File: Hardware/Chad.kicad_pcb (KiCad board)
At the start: 4 copper layers, 30 x 60 mm, 127 parts, among them J1 RBUS, J2 GPIO Breakout, J3 ServoCH1, J4 ServoCH2, J5 USB_C_Receptacle_USB2.0, U1 ESP32-S3, U2 SN65HVD230, U3 LM66200DRLR, U4 MAX77827AEFD+T, U5 SC4215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

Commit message: last commit is a lie, made some small changes
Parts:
- moved LOGO1 0.56 mm to (49.4, 82.0)
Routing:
- net GND: track 24.8 -> 30.5 mm
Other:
- board text added: "JLCJLCJLCJLC"
- board text added: "Serial Number -"

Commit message: small silkscreen tweaks
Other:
- board text added: "C.H.A.D-v2.0"
- board text removed: "C.H.A.D-v2"
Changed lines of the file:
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@@
   (gr_line locked (start 62 99.09) (end 62 45.09)
     (stroke (width 0.1) (type solid)) (layer "Edge.Cuts"))
-  (gr_text "Serial Number - " (at 59.85 93.3 -90) (layer "B.SilkS")
-    (effects (font (size 0.7 0.7) (thickness 0.1524) bold) (justify left bottom mirror))
+  (gr_text "Serial Number - " (at 59.81 95.7 270) (layer "B.SilkS")
+    (effects (font (size 0.9 0.9) (thickness 0.1524) bold) (justify left bottom mirror))
   )
-  (gr_text "JLCJLCJLCJLC" (at 59.78 84.39 -90) (layer "B.SilkS")
-    (effects (font (size 0.7 0.7) (thickness 0.1524) bold) (justify left bottom mirror))
+  (gr_text "JLCJLCJLCJLC" (at 59.76 84.05 270) (layer "B.SilkS")
+    (effects (font (size 0.9 0.9) (thickness 0.1524) bold) (justify left bottom mirror))
   )
-  (gr_text "C.H.A.D-v2\n" (at 58.35 89.275) (layer "B.SilkS")
-    (effects (font (size 1.8 1.8) (thickness 0.25)) (justify left mirror))
+  (gr_text "C.H.A.D-v2.0\n" (at 59.39 89.34) (layer "B.SilkS")
+    (effects (font (size 1.7 1.7) (thickness 0.25)) (justify left mirror))
   )
-  (gr_text "Designed By\nAndrei Paduraru\nElectronics and Payload 2023" (at 47.15 94.05) (layer "B.SilkS")
+  (gr_text "Designed By\nAndrei Paduraru\nElectronics and Payload 2023" (at 47.11 94.08) (layer "B.SilkS")
     (effects (font (size 1 1) (thickness 0.2)) (justify mirror))
   )

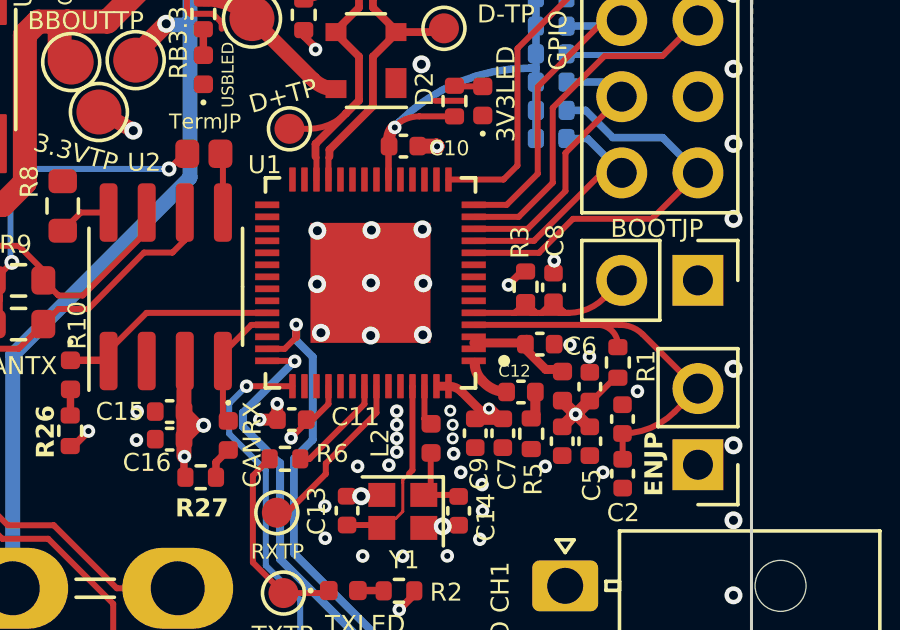
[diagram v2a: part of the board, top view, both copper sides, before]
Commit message: better ICLR logo, 3d model exports with edge connectors
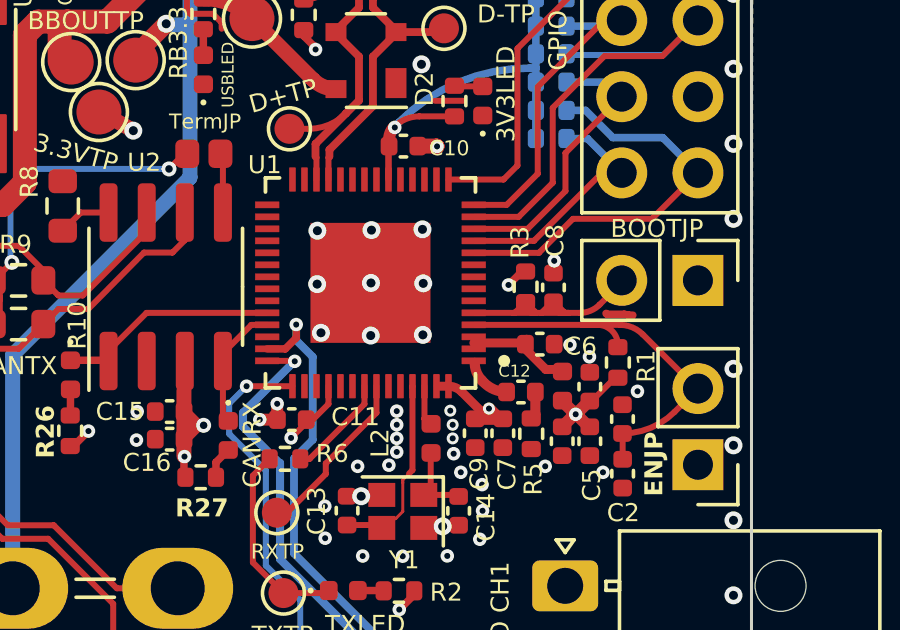
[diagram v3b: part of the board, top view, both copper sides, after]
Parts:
- LOGO1: footprint iclr:iclr_logo -> iclr:iclr_logo_estd2018_10mm
- moved LOGO1 0.44 mm to (49.6, 82.4)
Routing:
- net GND: track 30.5 -> 31.4 mm
